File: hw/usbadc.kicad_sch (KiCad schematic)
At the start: 11 parts, among them U6 PCA9306, U8 24AA0x, X1 ECS-2520MV-260-CN-TR

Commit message: WIP; converging
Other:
- sheet FPGA Trion ports: added CDON; removed CDONb
- sheet LEDs ports: added LED_CDON; removed LED_DONb
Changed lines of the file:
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@@
       (effects (font (size 1.27 1.27)) (justify left top))
-    )
-    (pin "LED_DONb" input (at 259.08 54.61 180)
-      (effects (font (size 1.27 1.27)) (justify left))
     )
     (pin "LED_CHB_B" input (at 259.08 94.615 180)
@@
     )
     (pin "LED_FL_R" input (at 259.08 99.06 180)
+      (effects (font (size 1.27 1.27)) (justify left))
+    )
+    (pin "LED_CDON" input (at 259.08 54.61 180)
       (effects (font (size 1.27 1.27)) (justify left))
     )
@@
       (effects (font (size 1.27 1.27)) (justify left top))
     )
-    (pin "CDONb" output (at 227.33 54.61 0)
+    (pin "CDON" output (at 227.33 54.61 0)
       (effects (font (size 1.27 1.27)) (justify right))
     )

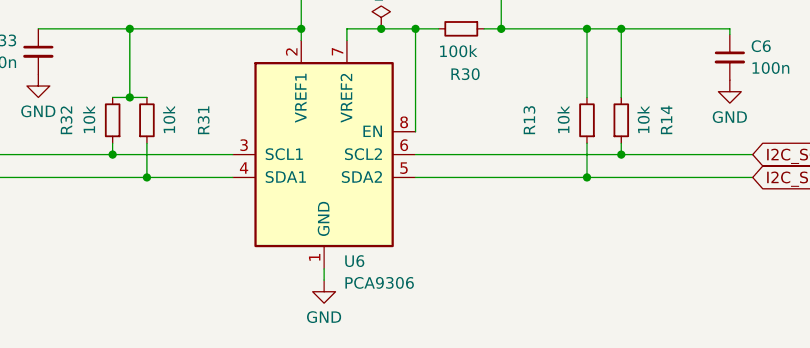
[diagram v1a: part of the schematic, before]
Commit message: updated some component values
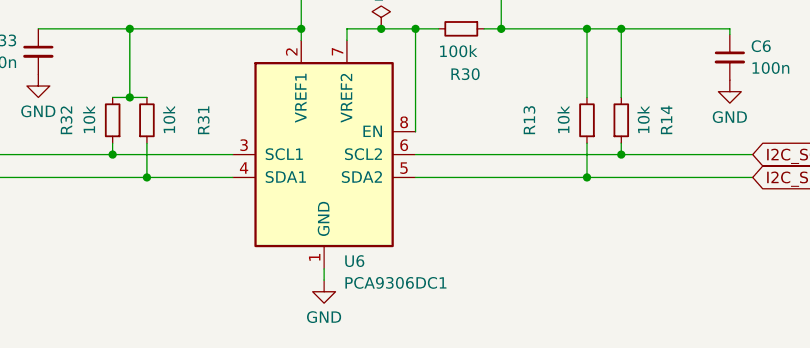
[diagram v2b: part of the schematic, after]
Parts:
- U6: value PCA9306 -> PCA9306DC1
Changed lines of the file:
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@@
       (effects (font (size 1.27 1.27)) (justify left))
     )
-    (property "Value" "PCA9306" (at 79.0291 192.7393 0)
+    (property "Value" "PCA9306DC1" (at 79.0291 192.7393 0)
       (effects (font (size 1.27 1.27)) (justify left))
     )

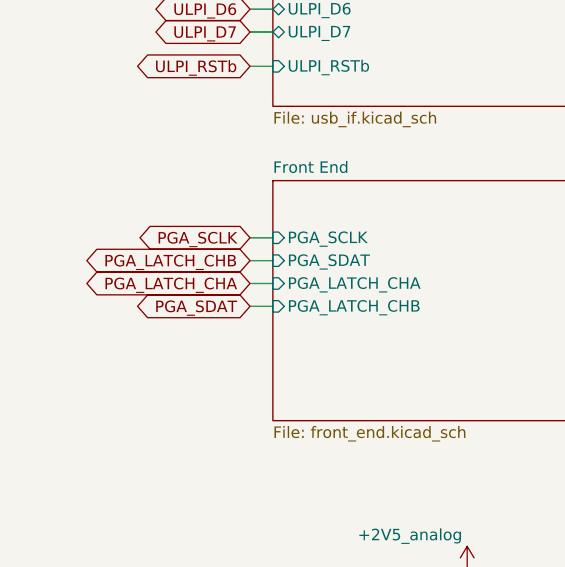
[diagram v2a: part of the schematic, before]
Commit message: PGA_SDAT / PGA_LATCH_CHB were swapped in top-sheet
 -> corrected there and swapped at FPGA bank keeps the
 layout unmodified but fixes the labels.
 => still compatible with v3.0 as ordered from JLC
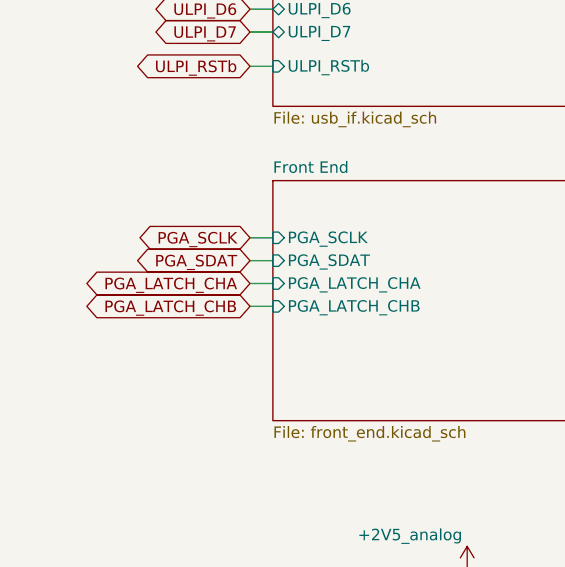
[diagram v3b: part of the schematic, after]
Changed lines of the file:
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@@
     (effects (font (size 1.27 1.27)) (justify left bottom))
   )
-  (global_label "PGA_SDAT" (shape bidirectional) (at 50.165 129.54 180) (fields_autoplaced)
-    (effects (font (size 1.27 1.27)) (justify right))
-    (property "Intersheetrefs" "${INTERSHEET_REFS}" (at 37.7496 129.54 0)
+  (global_label "PGA_SDAT" (shape bidirectional) (at 50.165 124.46 180) (fields_autoplaced)
+    (effects (font (size 1.27 1.27)) (justify right))
+    (property "Intersheetrefs" "${INTERSHEET_REFS}" (at 37.7496 124.46 0)
       (effects (font (size 1.27 1.27)) (justify right) hide)
     )
@@
     )
   )
-  (global_label "PGA_LATCH_CHB" (shape bidirectional) (at 50.165 124.46 180) (fields_autoplaced)
-    (effects (font (size 1.27 1.27)) (justify right))
-    (property "Intersheetrefs" "${INTERSHEET_REFS}" (at 31.7624 124.46 0)
-      (effects (font (size 1.27 1.27)) (justify right) hide)
-    )
+  (global_label "PGA_LATCH_CHB" (shape bidirectional) (at 50.165 129.54 180) (fields_autoplaced)
+    (effects (font (size 1.27 1.27)) (justify right))
+    (property "Intersheetrefs" "${INTERSHEET_REFS}" (at 31.7624 129.54 0)
+      (effects (font (size 1.27 1.27)) (justify right) hide)
+    )

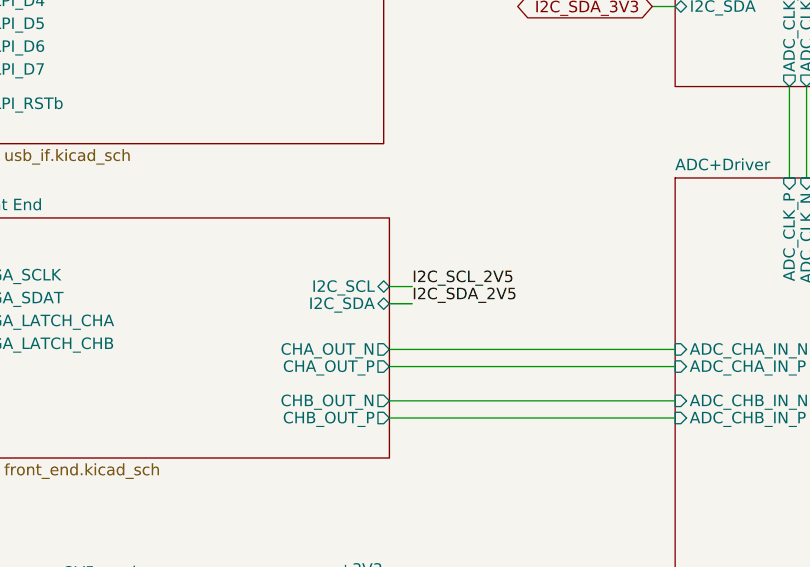
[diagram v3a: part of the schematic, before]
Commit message: Connected FEC i2c to 3V3
This permits omitting the i2c level converted if the DAC is not used.
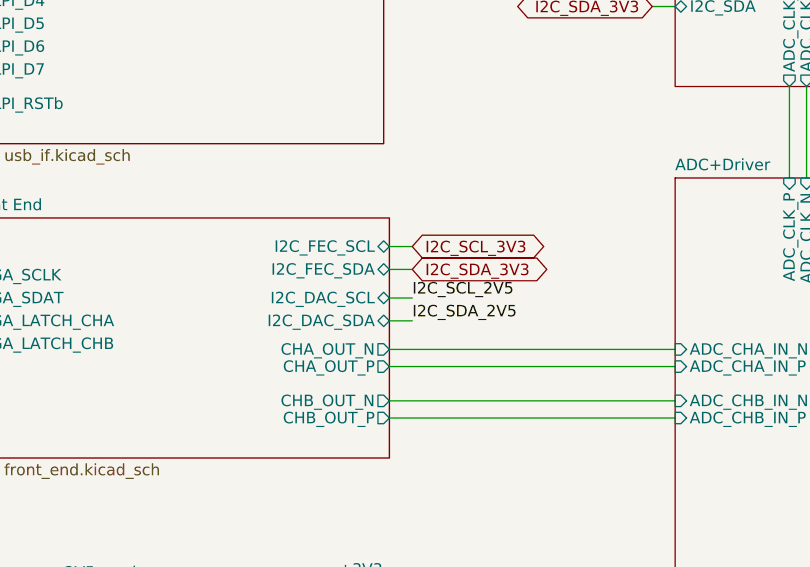
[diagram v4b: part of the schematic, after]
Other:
- sheet Front End ports: added I2C_DAC_SCL, I2C_DAC_SDA, I2C_FEC_SCL, I2C_FEC_SDA; removed I2C_SCL, I2C_SDA
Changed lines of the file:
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@@
+    (stroke (width 0) (type default))
+  )
+  (wire (pts (xy 99.695 118.745) (xy 102.235 118.745))
     (stroke (width 0) (type default))
   )
@@
     (stroke (width 0) (type default))
   )
-  (wire (pts (xy 99.695 123.19) (xy 102.235 123.19))
+  (wire (pts (xy 99.695 124.46) (xy 102.235 124.46))
     (stroke (width 0) (type default))
   )
@@
     (stroke (width 0) (type default))
   )
-  (wire (pts (xy 99.695 125.095) (xy 102.235 125.095))
+  (wire (pts (xy 99.695 127) (xy 102.235 127))
     (stroke (width 0) (type default))
   )
@@
     (stroke (width 0) (type default))
   )
+  (wire (pts (xy 99.695 121.285) (xy 102.235 121.285))
+    (stroke (width 0) (type default))
+  )
   (wire (pts (xy 215.265 120.015) (xy 215.265 121.285))
     (stroke (width 0) (type default))
@@
     (stroke (width 0) (type default))
   )
-  (label "I2C_SCL_2V5" (at 102.235 123.19 0) (fields_autoplaced)
+  (label "I2C_SCL_2V5" (at 102.235 124.46 0) (fields_autoplaced)
     (effects (font (size 1.27 1.27)) (justify left bottom))
   )
@@
     (effects (font (size 1.27 1.27)) (justify right bottom))
   )
-  (label "I2C_SDA_2V5" (at 102.235 125.095 0) (fields_autoplaced)
+  (label "I2C_SDA_2V5" (at 102.235 127 0) (fields_autoplaced)
     (effects (font (size 1.27 1.27)) (justify left bottom))
   )
@@
     )
   )
+  (global_label "I2C_SDA_3V3" (shape bidirectional) (at 102.235 121.285 0) (fields_autoplaced)
+    (effects (font (size 1.27 1.27)) (justify left))
+    (property "Intersheetrefs" "${INTERSHEET_REFS}" (at 117.6137 121.285 0)
+      (effects (font (size 1.27 1.27)) (justify left) hide)
+    )
+  )
   (global_label "ADC_SYNC" (shape bidirectional) (at 170.815 118.745 0) (fields_autoplaced)
     (effects (font (size 1.27 1.27)) (justify left))
@@
     (effects (font (size 1.27 1.27)) (justify left))
     (property "Intersheetrefs" "${INTERSHEET_REFS}" (at 139.7782 178.435 0)
+      (effects (font (size 1.27 1.27)) (justify left) hide)
+    )
+  )
+  (global_label "I2C_SCL_3V3" (shape bidirectional) (at 102.235 118.745 0) (fields_autoplaced)
+    (effects (font (size 1.27 1.27)) (justify left))
+    (property "Intersheetrefs" "${INTERSHEET_REFS}" (at 117.5532 118.745 0)
       (effects (font (size 1.27 1.27)) (justify left) hide)
     )
@@
       (effects (font (size 1.27 1.27)) (justify left top))
     )
-    (pin "I2C_SDA" bidirectional (at 99.695 125.095 0)
-      (effects (font (size 1.27 1.27)) (justify right))
-    )
     (pin "CHB_OUT_N" output (at 99.695 135.89 0)
       (effects (font (size 1.27 1.27)) (justify right))
@@
       (effects (font (size 1.27 1.27)) (justify right))
     )
-    (pin "I2C_SCL" bidirectional (at 99.695 123.19 0)
-      (effects (font (size 1.27 1.27)) (justify right))
-    )
     (pin "PGA_SDAT" input (at 52.705 124.46 180)
       (effects (font (size 1.27 1.27)) (justify left))
@@
       (effects (font (size 1.27 1.27)) (justify right))
     )
+    (pin "I2C_DAC_SDA" bidirectional (at 99.695 127 0)
+      (effects (font (size 1.27 1.27)) (justify right))
+    )
+    (pin "I2C_DAC_SCL" bidirectional (at 99.695 124.46 0)
+      (effects (font (size 1.27 1.27)) (justify right))
+    )
+    (pin "I2C_FEC_SDA" bidirectional (at 99.695 121.285 0)
+      (effects (font (size 1.27 1.27)) (justify right))
+    )
+    (pin "I2C_FEC_SCL" bidirectional (at 99.695 118.745 0)
+      (effects (font (size 1.27 1.27)) (justify right))
+    )

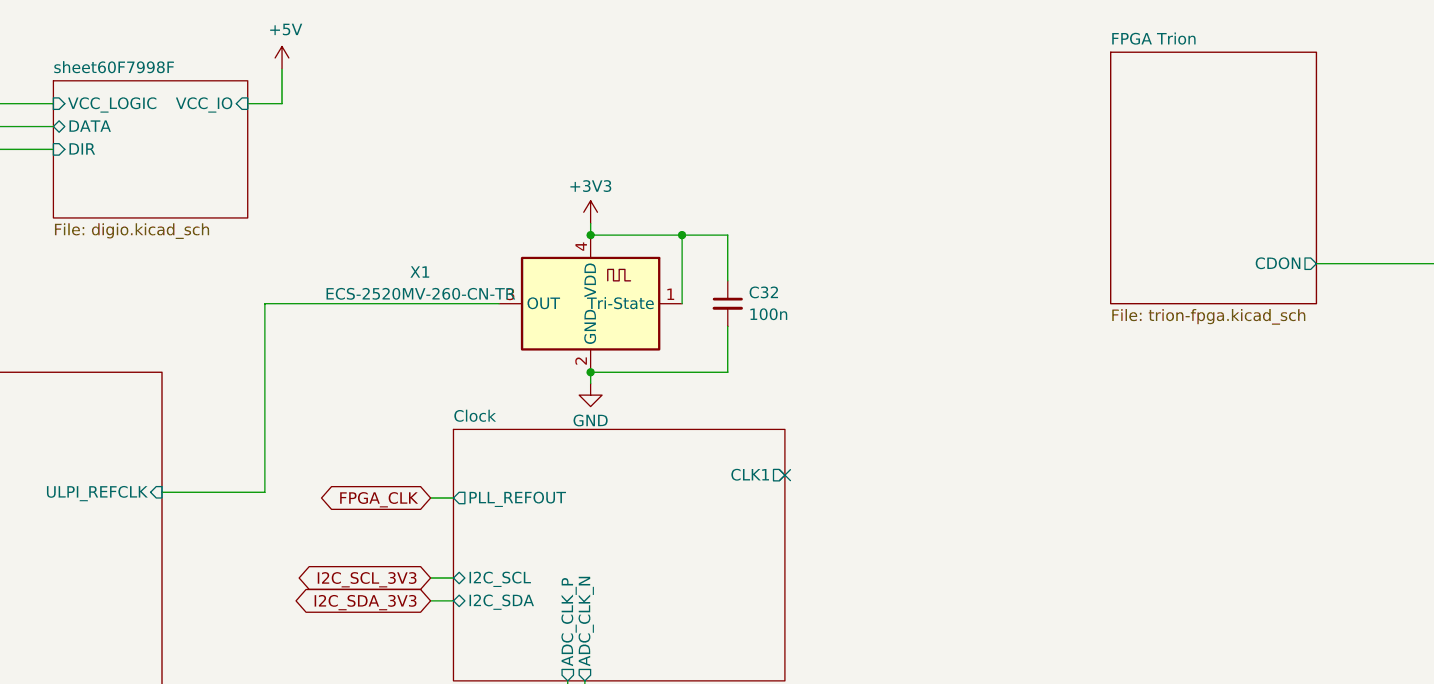
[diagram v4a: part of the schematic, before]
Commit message: Added (optional) connection from PLL output 4 to ulpi refclock.
Could spare the crystal oscillator...
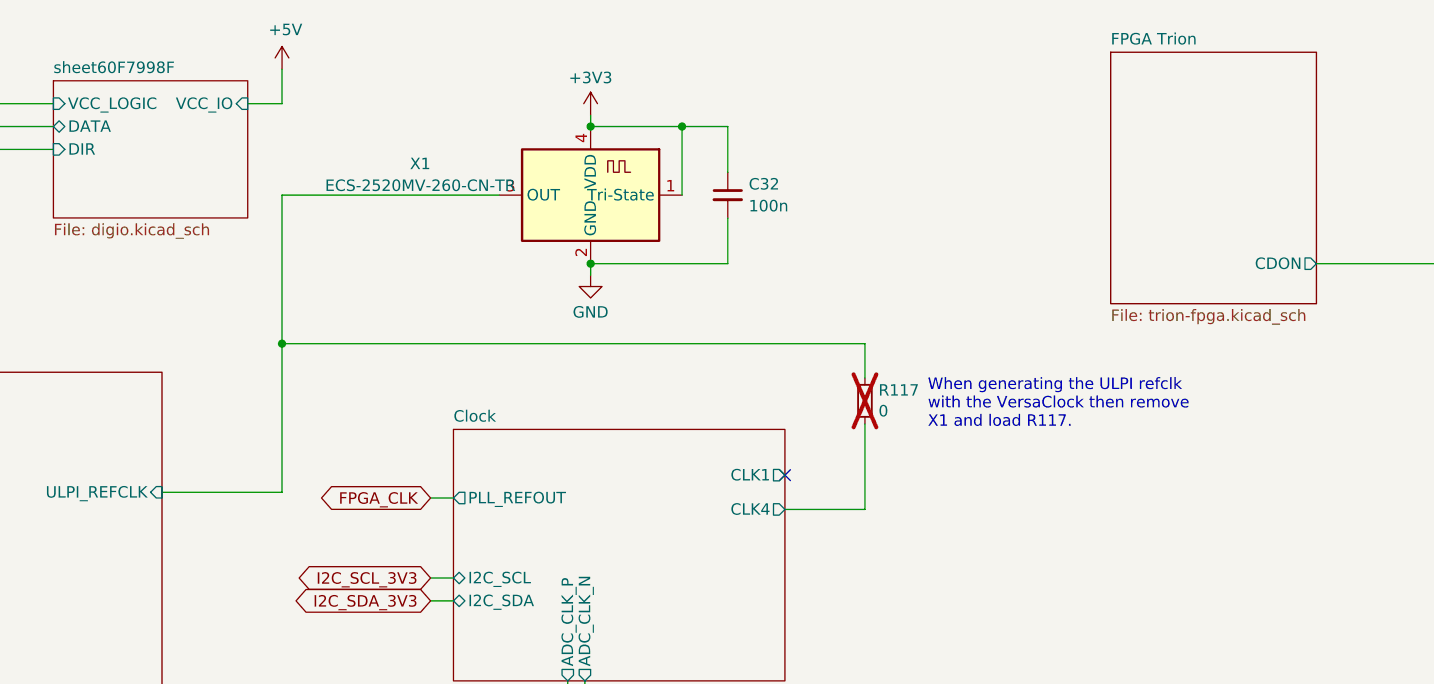
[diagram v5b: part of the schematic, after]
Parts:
- added R117: 0, Resistor_SMD:R_0603_1608Metric, symbol Device:R_Small
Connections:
- net USB/ULPI_REFCLK: now also R117.1
- new net Clock/CLK4: R117.2
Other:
- sheet Clock ports: added CLK4; removed none
- note added: "When generating the ULPI refclk with the VersaClock then remove X1 and load R117."
- moved on the sheet: C32, X1

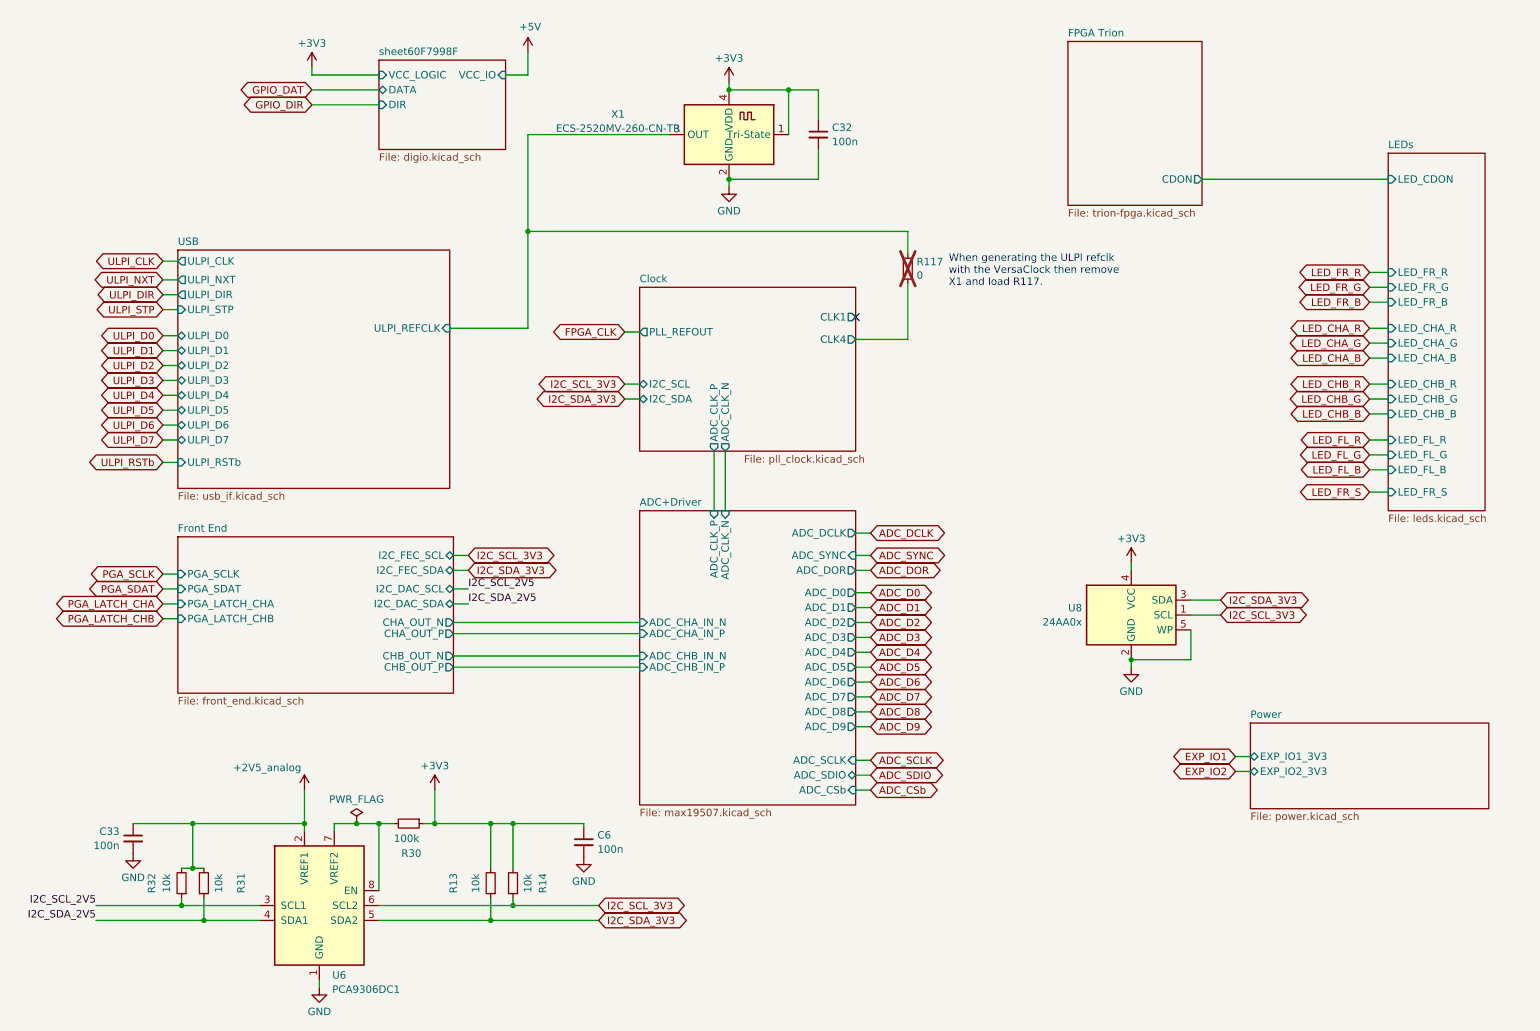
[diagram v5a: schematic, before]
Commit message: added jumperable VDDIO for digital I/O, added reset generator
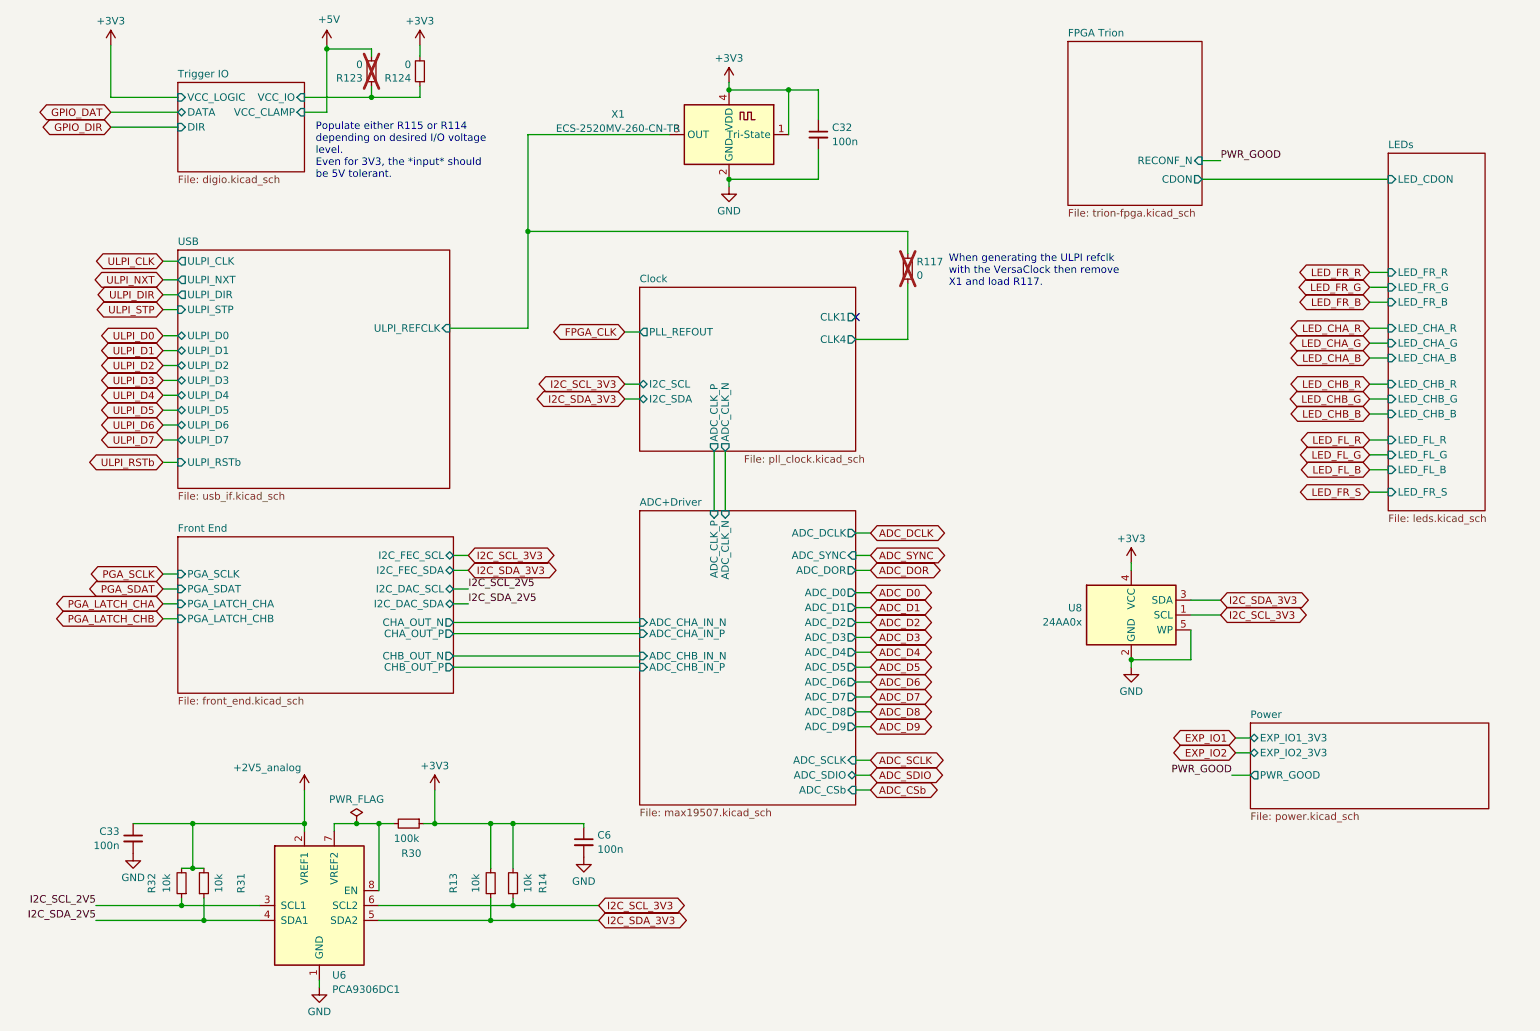
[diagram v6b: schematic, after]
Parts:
- added R123, R124: 0, Resistor_SMD:R_0603_1608Metric, symbol Device:R_Small
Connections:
- net +3V3: now also R124.2
- net +5V: now also R123.2
- new net Trigger IO/VCC_IO: R123.1, R124.1
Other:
- sheet sheet60F7998F renamed Trigger IO
- sheet FPGA Trion ports: added RECONF_N; removed none
- sheet Power ports: added PWR_GOOD; removed none
- sheet Trigger IO ports: added VCC_CLAMP; removed none
- note added: "Populate either R115 or R114 depending on desired I/O voltage level. Even for 3V3, the *input* should be 5V tolerant."
